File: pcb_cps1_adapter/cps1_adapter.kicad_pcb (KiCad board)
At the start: 2 copper layers, 31.1 x 63.5 mm, 34 parts, among them J1 Conn_02x05_Counter_Clockwise, J2 Conn_02x05_Counter_Clockwise, J3 Conn_02x05_Counter_Clockwise, J4 Conn_02x05_Counter_Clockwise, J5 Conn_02x05_Counter_Clockwise, U1 74LVC112, U2 WM8782

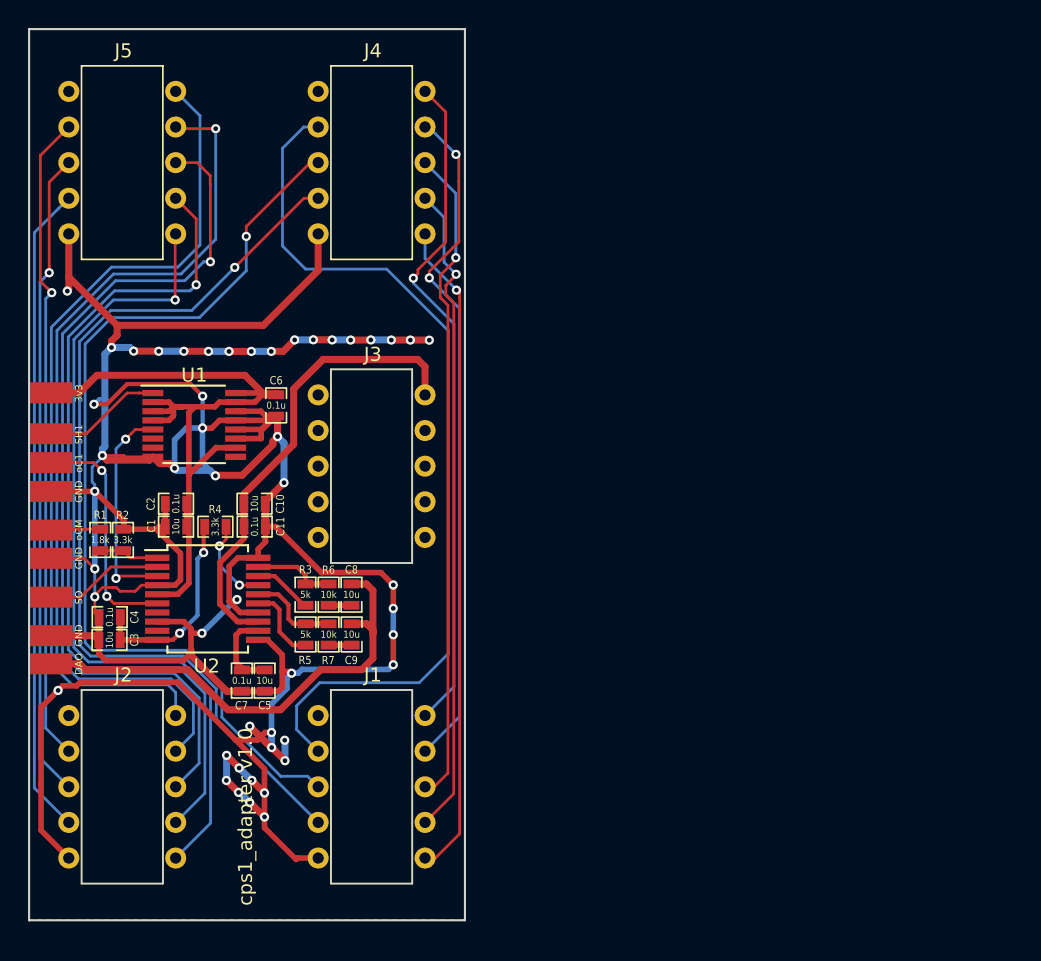
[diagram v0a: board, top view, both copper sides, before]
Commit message: update adapter board to version 1.1
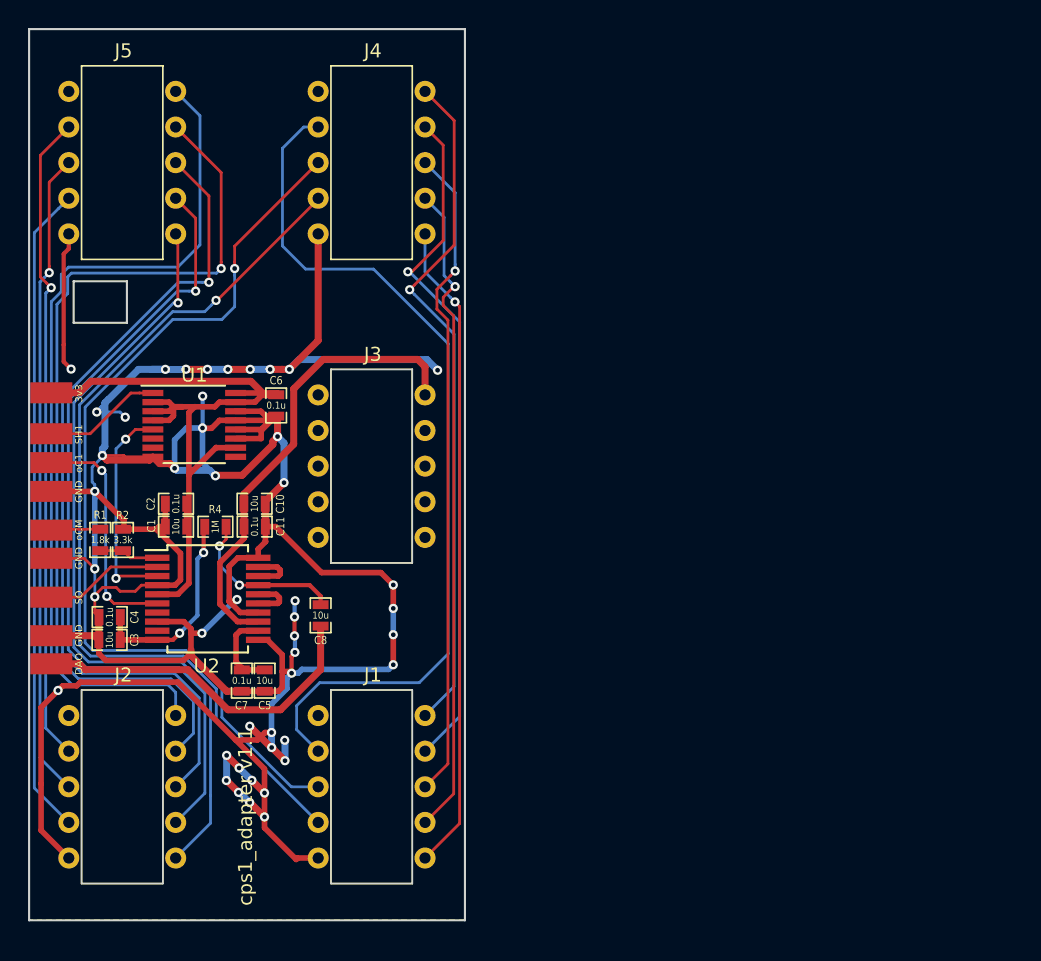
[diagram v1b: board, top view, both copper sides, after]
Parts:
- removed C9: 10u, custom_components:SM0603_Capa_libcms
- removed R3, R5: 5k, custom_components:SM0603_Resistor_libcms
- removed R6, R7: 10k, custom_components:SM0603_Resistor_libcms
- R4: value 3.3k -> 1M
- moved C8 2.65 mm to (61.4, 72.9), turned to 90 degrees
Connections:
- R4 pad 2: Net-(R4-Pad2) -> Net-(C8-Pad2)
- U2 pad 15: Net-(R5-Pad2) -> Net-(U2-Pad15)
- U2 pad 16: Net-(R5-Pad1) -> Net-(U2-Pad15)
- U2 pad 17: Net-(R4-Pad2) -> Net-(C8-Pad2)
- U2 pad 18: Net-(R3-Pad2) -> Net-(U2-Pad18)
- U2 pad 19: Net-(R3-Pad1) -> Net-(U2-Pad18)
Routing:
- net GND: track 294.0 -> 282.8 mm, vias 49 -> 46
- net Net-(C8-Pad2): track 1.63 -> 11.7 mm, vias 0 -> 2
- net /DAO: track 34.3 -> 24.9 mm
- net Net-(R5-Pad1): track 6.49 -> 0.00 mm
- net Net-(R4-Pad2): track 6.29 -> 0.00 mm, vias 2 -> 0
- net Net-(R3-Pad1): track 5.88 -> 0.00 mm
- net Net-(R5-Pad2): track 5.54 -> 0.00 mm
- net Net-(R3-Pad2): track 4.23 -> 0.00 mm
- net Net-(U2-Pad18): track 0.00 -> 3.58 mm
- net Net-(U2-Pad15): track 0.00 -> 3.46 mm
- net /F1: track 62.5 -> 59.7 mm
- net /B2: track 66.5 -> 63.9 mm
- net /F0: track 60.8 -> 58.4 mm
- net /R3: track 59.0 -> 56.8 mm
- net /B1: track 67.3 -> 65.3 mm
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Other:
- outline, holes or cut-outs redrawn
- board text added: "cps1_adapter v1.1"
- board text removed: "cps1_adapter v1.0"

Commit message: update cps1_adapter to version 1.2
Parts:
- removed TP5: GND, custom_components:SMD_PAD
- moved TP3 53.2 mm to (95.4, 58.1), turned to 270 degrees
- moved TP4 51.5 mm to (91.9, 58.1), turned to 270 degrees
- moved TP6 41.1 mm to (83.2, 59.4)
- moved TP7 41.1 mm to (83.2, 57.3)
- moved J1 39.0 mm to (100.2, 80.0)
- moved J2 39.0 mm to (82.4, 80.0)
- moved J3 39.0 mm to (100.2, 57.1)
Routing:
- net GND: track 282.8 -> 507.4 mm, vias 46 -> 76
- net /SO: track 8.44 -> 56.7 mm, vias 0 -> 2
- net /DVDD5V: track 33.2 -> 74.3 mm
- net /R0: track 46.5 -> 79.9 mm, vias 1 -> 0
- net /R1: track 46.2 -> 78.8 mm, vias 1 -> 0
- net /oC1: track 16.8 -> 47.8 mm
- net /R2: track 46.5 -> 76.0 mm
- net /DVDD3V3: track 54.2 -> 82.5 mm
- net /G1: track 46.9 -> 73.8 mm, vias 1 -> 0
- net /G0: track 47.0 -> 73.8 mm, vias 1 -> 0
- net /B3: track 46.5 -> 73.1 mm, vias 1 -> 0
- net /SH1: track 8.44 -> 34.6 mm
- net /G2: track 49.1 -> 74.1 mm, vias 1 -> 0
- net /G3: track 48.8 -> 73.1 mm, vias 1 -> 0
- net /R3: track 56.8 -> 68.8 mm, vias 1 -> 0
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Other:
- board size 31.1 x 63.5 mm -> 70.1 x 63.5 mm
- board text added: "(J3)"
- board text added: "(J5)"
- board text added: "(VS)"
- board text added: "cps1_adapter v1.2 (89626A compatible)"
- board text removed: "cps1_adapter v1.1"
